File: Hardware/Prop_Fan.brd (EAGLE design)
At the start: 152.9 x 71.1 mm, 161 parts, among them J1 1546215-2, J2 1546215-2, J3 1546215-2, J4 1546215-2, J5 1546215-2, SW1 MF-SW-TACT-4.2MM, SW2 MF-SW-TACT-4.2MM, SW3 MF-SW-TACT-4.2MM, U1 P8X32A-Q44, U10 MAX31855KASA+, U11 MAX31855KASA+, U12 G3VM-61GR2(TR05), U13 G3VM-61GR2(TR05), U14 CD74HC595M96, U15 G3VM-61GR2(TR05), U16 CD74HC165M96, U17 G3VM-61GR2(TR05), U18 G3VM-61GR2(TR05), U19 G3VM-61GR2(TR05), U2 G3VM-61GR2(TR05), U20 G3VM-61GR2(TR05), U21 G3VM-61GR2(TR05), U22 G3VM-61GR2(TR05), U23 G3VM-61GR2(TR05), U24 G3VM-61GR2(TR05), U25 G3VM-61GR2(TR05), U26 G3VM-61GR2(TR05), U27 FXOS8700CQR1, U28 ACPL-C870-000E, U29 MAX11613EUA+, U3 G3VM-61GR2(TR05), U30 TPS7B6950QDBVRQ1, U4 MAX31855KASA+, U5 LM22678TJ-5.0/NOPB, U6 ADP3338AKCZ-3.3-RL, U7 CAT24C512WI-GT3, U8 G3VM-61GR2(TR05), U9 MAX31855KASA+, X1 ABMM-6.000MHZ-B2-T

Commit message: Fixed a couple traces and added camfiles.
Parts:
- added U$35: JEEP_LOGO_SILK_MEDIUM, PP_Aesthetics:JEEP_SILK_MEDIUM
- added U$42: LHE_LOGOLHE_LOGO, PP_Aesthetics:LHE_LOGO
- moved U$1 25.2 mm to (46.5, 15.2)
- moved TP2 12.4 mm to (20.3, 51.6)
- moved C22 3.05 mm to (23.4, 45.2)
- moved C23 3.05 mm to (23.4, 41.4)
- moved 3.3V_PWR 2.55 mm to (29.2, 39.4)
- moved R11 2.55 mm to (25.4, 39.4)
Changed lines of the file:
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@@
 <?xml version="1.0" encoding="utf-8"?>
 <!DOCTYPE eagle SYSTEM "eagle.dtd">
-<eagle version="7.4.0">
+<eagle version="6.6.0">
 <drawing>
 <settings>
@@
 <pass name="Default">
 <param name="RoutingGrid" value="50mil"/>
-<param name="AutoGrid" value="1"/>
-<param name="Efforts" value="0"/>
-<param name="TopRouterVariant" value="1"/>
 <param name="tpViaShape" value="round"/>
 <param name="PrefDir.1" value="|"/>
@@
 <attribute name="NAME" x="5.168" y="38.298" size="0.8128" layer="25" font="vector" ratio="16"/>
 </element>
-<element name="C22" library="PP_Passives" package="1210" value="10uF" x="23.436" y="48.21"/>
-<element name="C23" library="PP_Passives" package="0805" value="0.1uF" x="23.436" y="44.44"/>
+<element name="C22" library="PP_Passives" package="1210" value="10uF" x="23.436" y="45.162"/>
+<element name="C23" library="PP_Passives" package="0805" value="0.1uF" x="23.436" y="41.392"/>
 <element name="C24" library="PP_Passives" package="6.3MM_CAP_SMD" value="UWJ1C470MCL1GB" x="13.902" y="53.362" smashed="yes" rot="R270">
 <attribute name="NAME" x="10.648" y="56.895" size="0.8128" layer="25" font="vector" ratio="16"/>
 </element>
-<element name="3.3V_PWR" library="PP_LED" package="LED_0805" value="MF-LED-0805-RED" x="28.956" y="41.91" smashed="yes" rot="R180">
-<attribute name="NAME" x="26.585" y="43.18" size="0.8128" layer="25" font="vector" ratio="16"/>
-</element>
-<element name="R11" library="PP_Passives" package="0603" value="330" x="25.146" y="41.91" smashed="yes" rot="R180">
-<attribute name="NAME" x="23.5458" y="40.132" size="0.8128" layer="25" font="vector" ratio="16"/>
+<element name="3.3V_PWR" library="PP_LED" package="LED_0805" value="MF-LED-0805-RED" x="29.21" y="39.37" smashed="yes" rot="R180">
+<attribute name="NAME" x="26.839" y="40.64" size="0.8128" layer="25" font="vector" ratio="16"/>
+</element>
+<element name="R11" library="PP_Passives" package="0603" value="330" x="25.4" y="39.37" smashed="yes" rot="R180">
+<attribute name="NAME" x="21.2598" y="38.862" size="0.8128" layer="25" font="vector" ratio="16"/>
 </element>
 <element name="TP1" library="PP_Connectors" package="KEYSTONE_5115-5119" value="5115-5119" x="34.036" y="3.048" smashed="yes" rot="R90">
 <attribute name="NAME" x="33.02" y="5.842" size="0.8128" layer="25" font="vector" ratio="16"/>
 </element>
-<element name="TP2" library="PP_Connectors" package="KEYSTONE_5115-5119" value="5115-5119" x="20.574" y="39.116" smashed="yes">
-<attribute name="NAME" x="18.034" y="41.91" size="0.8128" layer="25" font="vector" ratio="16"/>
+<element name="TP2" library="PP_Connectors" package="KEYSTONE_5115-5119" value="5115-5119" x="20.32" y="51.562" smashed="yes">
+<attribute name="NAME" x="22.86" y="53.34" size="0.8128" layer="25" font="vector" ratio="16"/>
 </element>
 <element name="TP3" library="PP_Connectors" package="KEYSTONE_5115-5119" value="5115-5119" x="81.788" y="2.858" rot="R180"/>
@@
 </element>
 <element name="R15" library="PP_Passives" package="0805" value="10K" x="51.816" y="36.322" smashed="yes" rot="R270">
-<attribute name="NAME" x="48.768" y="36.83" size="0.8128" layer="25" font="vector" ratio="16"/>
+<attribute name="NAME" x="52.07" y="32.258" size="0.8128" layer="25" font="vector" ratio="16" rot="R90"/>
 </element>
 <element name="R16" library="PP_Passives" package="0805" value="10K" x="53.848" y="36.322" smashed="yes" rot="R270">
@@
 <element name="R10" library="PP_Passives" package="0805" value="10K" x="76.962" y="57.404" rot="R180"/>
 <element name="R17" library="PP_Passives" package="0805" value="10K" x="68.834" y="57.404" rot="R180"/>
-<element name="U$1" library="PP_Aesthetics" package="LHE_FRAME" value="LHE_FRAME" x="27.432" y="31.75">
-<attribute name="DNAME" value="Parker Dillmann" x="27.432" y="31.75" size="1.778" layer="27" display="off"/>
-<attribute name="REVNUM" value="REV: 1" x="27.432" y="31.75" size="1.778" layer="27" display="off"/>
+<element name="U$1" library="PP_Aesthetics" package="LHE_FRAME" value="LHE_FRAME" x="46.482" y="15.24">
+<attribute name="DNAME" value="Parker Dillmann" x="46.482" y="15.24" size="1.778" layer="27" display="off"/>
+<attribute name="REVNUM" value="REV: 1" x="46.482" y="15.24" size="1.778" layer="27" display="off"/>
 </element>
 <element name="FID1" library="MF_Aesthetics" package="FIDUCIAL_0.5MM" value="FIDUCIAL_0.5MM" x="7.62" y="60.198"/>
@@
 <element name="C45" library="PP_Passives" package="1210" value="10uF" x="149.352" y="32.004"/>
 <element name="U30" library="MF_IC_Power" package="SOT-23-5" value="TPS7B6950QDBVRQ1" x="149.352" y="27.94" rot="R90"/>
+<element name="U$35" library="PP_Aesthetics" package="JEEP_SILK_MEDIUM" value="JEEP_LOGO_SILK_MEDIUM" x="23.622" y="28.448"/>
+<element name="U$42" library="PP_Aesthetics" package="LHE_LOGO" value="LHE_LOGOLHE_LOGO" x="63.754" y="15.24"/>
 </elements>
 <signals>
@@
 <via x="11.938" y="40.386" extent="1-16" drill="0.5"/>
 <wire x1="11.938" y1="40.386" x2="11.938" y2="40.64" width="0.6096" layer="16"/>
-<wire x1="24.836" y1="48.21" x2="26.67" y2="48.21" width="0.6096" layer="1"/>
-<wire x1="26.67" y1="48.21" x2="26.67" y2="48.26" width="0.6096" layer="1"/>
-<via x="26.67" y="48.26" extent="1-16" drill="0.5"/>
-<wire x1="26.67" y1="48.26" x2="26.67" y2="48.514" width="0.6096" layer="16"/>
-<wire x1="24.336" y1="44.44" x2="25.654" y2="44.44" width="0.6096" layer="1"/>
-<wire x1="25.654" y1="44.44" x2="25.654" y2="44.45" width="0.6096" layer="1"/>
-<via x="25.654" y="44.45" extent="1-16" drill="0.5"/>
-<wire x1="25.654" y1="44.45" x2="25.654" y2="44.704" width="0.6096" layer="16"/>
+<wire x1="24.836" y1="45.162" x2="26.67" y2="45.162" width="0.6096" layer="1"/>
+<wire x1="26.67" y1="45.162" x2="26.67" y2="45.212" width="0.6096" layer="1"/>
+<via x="26.67" y="45.212" extent="1-16" drill="0.5"/>
+<wire x1="26.67" y1="45.212" x2="26.67" y2="45.466" width="0.6096" layer="16"/>
+<wire x1="24.336" y1="41.392" x2="25.654" y2="41.392" width="0.6096" layer="1"/>
+<wire x1="25.654" y1="41.392" x2="25.654" y2="41.402" width="0.6096" layer="1"/>
+<via x="25.654" y="41.402" extent="1-16" drill="0.5"/>
+<wire x1="25.654" y1="41.402" x2="25.654" y2="41.656" width="0.6096" layer="16"/>
 <polygon width="0.254" layer="1" isolate="0.3048" thermals="no">
 <vertex x="98.552" y="11.938"/>
@@
 <via x="77.724" y="14.351" extent="1-16" drill="0.5"/>
 <via x="77.724" y="15.621" extent="1-16" drill="0.5"/>
-<wire x1="30.006" y1="41.91" x2="31.242" y2="41.91" width="0.254" layer="1"/>
-<via x="31.242" y="41.91" extent="1-16" drill="0.5"/>
-<wire x1="31.242" y1="41.91" x2="31.242" y2="42.418" width="0.254" layer="16"/>
+<wire x1="30.26" y1="39.37" x2="31.496" y2="39.37" width="0.254" layer="1"/>
+<via x="31.496" y="39.37" extent="1-16" drill="0.5"/>
+<wire x1="31.496" y1="39.37" x2="31.496" y2="39.878" width="0.254" layer="16"/>
 <contactref element="C25" pad="2"/>
 <contactref element="U27" pad="P$16"/>
@@
 <vertex x="7.874" y="46.228"/>
 </polygon>
-<wire x1="24.296" y1="41.91" x2="22.606" y2="41.91" width="0.254" layer="1"/>
+<wire x1="24.55" y1="39.37" x2="22.606" y2="39.37" width="0.254" layer="1"/>
 <contactref element="U27" pad="P$1"/>
 <contactref element="C25" pad="1"/>
@@
 <wire x1="133.096" y1="34.29" x2="133.096" y2="34.925" width="0.254" layer="1"/>
 <polygon width="0.254" layer="16" thermals="no">
-<vertex x="20.512371875" y="38.1" curve="-90"/>
-<vertex x="19.558" y="39.054371875"/>
-<vertex x="19.558" y="50.437965625"/>
-<vertex x="26.778034375" y="57.658"/>
+<vertex x="24.13" y="56.642"/>
+<vertex x="25.508034375" y="57.912"/>
 <vertex x="90.424" y="57.658"/>
 <vertex x="93.472" y="54.61"/>
@@
 <vertex x="92.456" y="54.102"/>
 <vertex x="89.916" y="56.642"/>
-<vertex x="28.194" y="56.642"/>
-<vertex x="21.59" y="50.038"/>
-<vertex x="21.59" y="39.177628125" curve="-90"/>
 </polygon>
 <wire x1="41.148" y1="52.186" x2="37.222" y2="52.186" width="0.254" layer="1"/>
@@
 <wire x1="140.716" y1="39.37" x2="138.4935" y2="39.37" width="0.254" layer="16"/>
 <wire x1="138.4935" y1="39.37" x2="138.43" y2="39.4335" width="0.254" layer="16"/>
+<polygon width="0.254" layer="16" isolate="0.3048" thermals="no">
+<vertex x="25.4" y="57.912"/>
+<vertex x="19.53925625" y="52.05125625" curve="45"/>
+<vertex x="19.304" y="51.483296875" curve="90"/>
+<vertex x="20.241296875" y="50.546" curve="45"/>
+<vertex x="20.80925625" y="50.78125625"/>
+<vertex x="26.67" y="56.642"/>
+<vertex x="26.67" y="57.912"/>
+</polygon>
 </signal>
 <signal name="X1">
@@
 <contactref element="R11" pad="1"/>
 <contactref element="3.3V_PWR" pad="ANODE"/>
-<wire x1="25.996" y1="41.91" x2="27.906" y2="41.91" width="0.254" layer="1"/>
+<wire x1="26.25" y1="39.37" x2="28.16" y2="39.37" width="0.254" layer="1"/>
 </signal>
 <signal name="N$2">

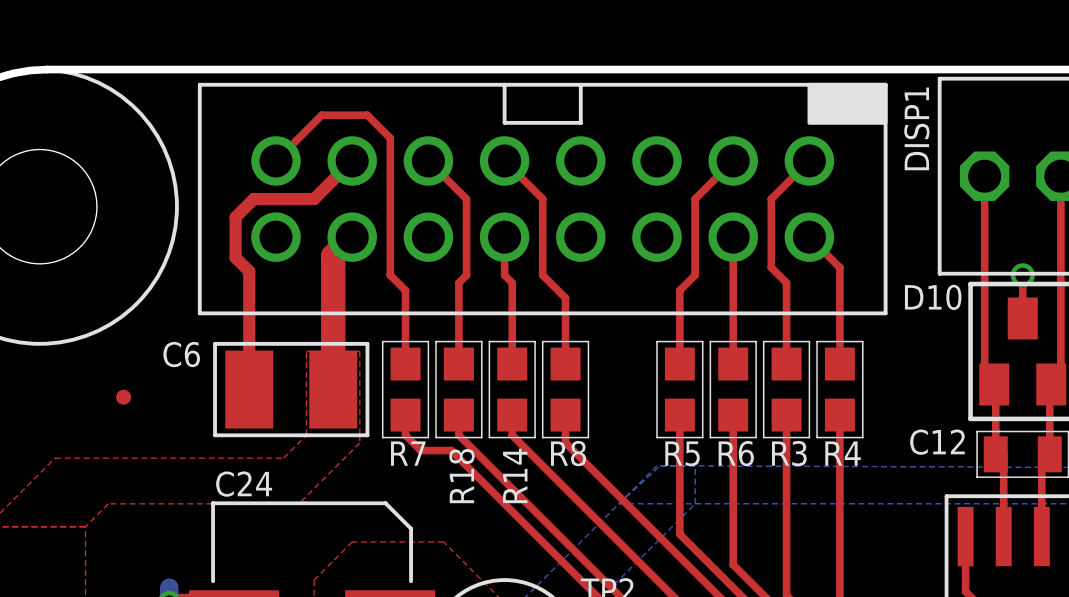
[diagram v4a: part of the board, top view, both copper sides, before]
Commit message: Fixed VFD connector. Was mirrored.
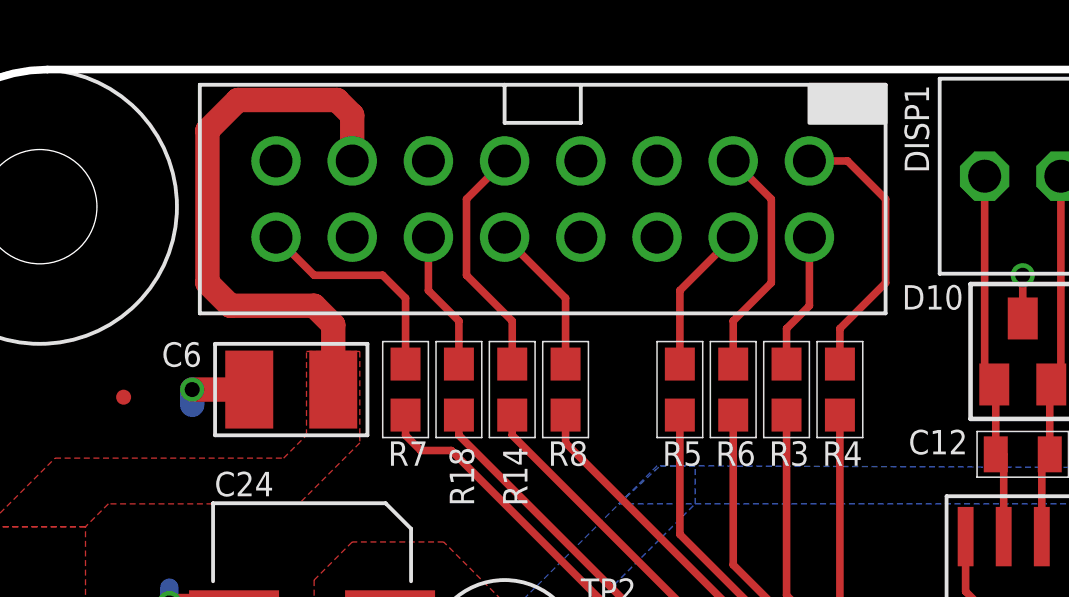
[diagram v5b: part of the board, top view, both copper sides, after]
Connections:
- net 5V_PWR: now also DISP1.P$13; no longer DISP1.P$14
- net D4: now also DISP1.P$3; no longer DISP1.P$4
- net D5: now also DISP1.P$4; no longer DISP1.P$3
- net D6: now also DISP1.P$1; no longer DISP1.P$2
- net D7: now also DISP1.P$2; no longer DISP1.P$1
- net E1: now also DISP1.P$10; no longer DISP1.P$9
- net E2: now also DISP1.P$16; no longer DISP1.P$15
- net GND: now also DISP1.P$14; no longer DISP1.P$13
- net R/W: now also DISP1.P$9; no longer DISP1.P$10
- net RS: now also DISP1.P$12; no longer DISP1.P$11
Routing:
- net 5V_PWR: track 14.7 -> 28.4 mm
- net GND: track 197.2 -> 189.0 mm, vias 138 -> 139
- net E2: track 12.5 -> 7.36 mm
- net D6: track 4.65 -> 9.20 mm
- net D4: track 4.23 -> 7.82 mm
- net R/W: track 4.34 -> 7.93 mm
- net D7: track 7.51 -> 4.55 mm
- net RS: track 7.40 -> 4.65 mm
- net D5: track 7.51 -> 4.97 mm
- net E1: track 7.61 -> 5.07 mm
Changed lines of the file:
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@@
 <?xml version="1.0" encoding="utf-8"?>
 <!DOCTYPE eagle SYSTEM "eagle.dtd">
-<eagle version="6.6.0">
+<eagle version="7.4.0">
 <drawing>
 <settings>
@@
 <pass name="Default">
 <param name="RoutingGrid" value="50mil"/>
+<param name="AutoGrid" value="1"/>
+<param name="Efforts" value="0"/>
+<param name="TopRouterVariant" value="1"/>
 <param name="tpViaShape" value="round"/>
 <param name="PrefDir.1" value="|"/>
@@
 <contactref element="PROP_UART" pad="1"/>
 <contactref element="PROP_TC" pad="P$5"/>
+<contactref element="DISP1" pad="P$7"/>
+<contactref element="DISP1" pad="P$5"/>
 <contactref element="DISP1" pad="P$8"/>
+<contactref element="DISP1" pad="P$14"/>
 <contactref element="DISP1" pad="P$6"/>
-<contactref element="DISP1" pad="P$7"/>
-<contactref element="DISP1" pad="P$13"/>
-<contactref element="DISP1" pad="P$5"/>
 <contactref element="C6" pad="2"/>
 <contactref element="U9" pad="1"/>
@@
 <via x="32.385" y="11.557" extent="1-16" drill="0.5"/>
 <via x="32.385" y="10.541" extent="1-16" drill="0.5"/>
-<wire x1="11.808" y1="60.452" x2="11.808" y2="64.392" width="0.4064" layer="1"/>
-<wire x1="11.808" y1="64.392" x2="11.35419375" y2="64.84580625" width="0.4064" layer="1"/>
-<wire x1="11.35419375" y1="64.84580625" x2="11.35419375" y2="66.19633125" width="0.4064" layer="1"/>
-<wire x1="11.35419375" y1="66.19633125" x2="11.9598625" y2="66.802" width="0.4064" layer="1"/>
-<wire x1="11.9598625" y1="66.802" x2="13.97" y2="66.802" width="0.4064" layer="1"/>
-<wire x1="13.97" y1="66.802" x2="15.24" y2="68.072" width="0.4064" layer="1"/>
 <wire x1="11.302" y1="53.362" x2="11.28" y2="53.34" width="0.6096" layer="1"/>
 <wire x1="11.28" y1="53.34" x2="9.144" y2="53.34" width="0.6096" layer="1"/>
@@
 <wire x1="143.637" y1="36.2835" x2="143.637" y2="34.417" width="0.254" layer="1"/>
 <wire x1="143.637" y1="34.417" x2="144.018" y2="34.036" width="0.254" layer="1"/>
+<wire x1="11.808" y1="60.452" x2="9.906" y2="60.452" width="0.8128" layer="1"/>
+<via x="9.906" y="60.452" extent="1-16" drill="0.5"/>
+<wire x1="9.906" y1="60.452" x2="9.906" y2="59.944" width="0.8128" layer="16"/>
 </signal>
 <signal name="3.3V">
@@
 <contactref element="L3" pad="1"/>
 <contactref element="U5" pad="P$6"/>
-<contactref element="DISP1" pad="P$14"/>
+<contactref element="DISP1" pad="P$13"/>
 <contactref element="C6" pad="1"/>
 <contactref element="C13" pad="1"/>
@@
 <wire x1="8.594" y1="37.79" x2="4.882" y2="37.79" width="0.8128" layer="1"/>
 <wire x1="4.882" y1="37.79" x2="4.826" y2="37.846" width="0.8128" layer="1"/>
-<wire x1="15.24" y1="65.532" x2="14.608" y2="64.9" width="0.8128" layer="1"/>
-<wire x1="14.608" y1="64.9" x2="14.608" y2="60.452" width="0.8128" layer="1"/>
 <polygon width="0.254" layer="1" isolate="0.3048" thermals="no">
 <vertex x="3.048" y="55.88"/>
@@
 <vertex x="6.35" y="55.88"/>
 </polygon>
+<wire x1="14.608" y1="60.452" x2="14.608" y2="62.608" width="0.8128" layer="1"/>
+<wire x1="14.608" y1="62.608" x2="13.97" y2="63.246" width="0.8128" layer="1"/>
+<wire x1="13.97" y1="63.246" x2="11.176" y2="63.246" width="0.8128" layer="1"/>
+<wire x1="11.176" y1="63.246" x2="10.414" y2="64.008" width="0.8128" layer="1"/>
+<wire x1="10.414" y1="64.008" x2="10.414" y2="69.088" width="0.8128" layer="1"/>
+<wire x1="10.414" y1="69.088" x2="11.43" y2="70.104" width="0.8128" layer="1"/>
+<wire x1="11.43" y1="70.104" x2="14.732" y2="70.104" width="0.8128" layer="1"/>
+<wire x1="14.732" y1="70.104" x2="15.24" y2="69.596" width="0.8128" layer="1"/>
+<wire x1="15.24" y1="69.596" x2="15.24" y2="68.072" width="0.8128" layer="1"/>
 </signal>
 <signal name="CHASSIS_GND">
@@
 </signal>
 <signal name="D7">
+<contactref element="DISP1" pad="P$2"/>
+<contactref element="R3" pad="2"/>
+<wire x1="29.718" y1="61.302" x2="29.718" y2="62.484" width="0.254" layer="1"/>
+<wire x1="29.718" y1="62.484" x2="30.48" y2="63.246" width="0.254" layer="1"/>
+<wire x1="30.48" y1="63.246" x2="30.48" y2="65.532" width="0.254" layer="1"/>
+</signal>
+<signal name="D6">
 <contactref element="DISP1" pad="P$1"/>
-<contactref element="R3" pad="2"/>
-<wire x1="29.718" y1="61.302" x2="29.718" y2="64.008" width="0.254" layer="1"/>
-<wire x1="29.718" y1="64.008" x2="29.21" y2="64.516" width="0.254" layer="1"/>
-<wire x1="29.21" y1="64.516" x2="29.21" y2="66.802" width="0.254" layer="1"/>
-<wire x1="29.21" y1="66.802" x2="30.48" y2="68.072" width="0.254" layer="1"/>
-</signal>
-<signal name="D6">
-<contactref element="DISP1" pad="P$2"/>
 <contactref element="R4" pad="2"/>
-<wire x1="31.496" y1="61.302" x2="31.496" y2="64.516" width="0.254" layer="1"/>
-<wire x1="31.496" y1="64.516" x2="30.48" y2="65.532" width="0.254" layer="1"/>
+<wire x1="31.496" y1="61.302" x2="31.496" y2="62.484" width="0.254" layer="1"/>
+<wire x1="31.496" y1="62.484" x2="33.02" y2="64.008" width="0.254" layer="1"/>
+<wire x1="33.02" y1="64.008" x2="33.02" y2="66.802" width="0.254" layer="1"/>
+<wire x1="33.02" y1="66.802" x2="31.75" y2="68.072" width="0.254" layer="1"/>
+<wire x1="31.75" y1="68.072" x2="30.48" y2="68.072" width="0.254" layer="1"/>
 </signal>
 <signal name="D5">
-<contactref element="DISP1" pad="P$3"/>
+<contactref element="DISP1" pad="P$4"/>
 <contactref element="R5" pad="2"/>
 <wire x1="26.162" y1="61.302" x2="26.162" y2="63.754" width="0.254" layer="1"/>
-<wire x1="26.162" y1="63.754" x2="26.67" y2="64.262" width="0.254" layer="1"/>
-<wire x1="26.67" y1="64.262" x2="26.67" y2="66.802" width="0.254" layer="1"/>
-<wire x1="26.67" y1="66.802" x2="27.94" y2="68.072" width="0.254" layer="1"/>
+<wire x1="26.162" y1="63.754" x2="27.94" y2="65.532" width="0.254" layer="1"/>
 </signal>
 <signal name="D4">
-<contactref element="DISP1" pad="P$4"/>
+<contactref element="DISP1" pad="P$3"/>
 <contactref element="R6" pad="2"/>
-<wire x1="27.94" y1="61.302" x2="27.94" y2="65.532" width="0.254" layer="1"/>
+<wire x1="27.94" y1="61.302" x2="27.94" y2="62.738" width="0.254" layer="1"/>
+<wire x1="27.94" y1="62.738" x2="29.21" y2="64.008" width="0.254" layer="1"/>
+<wire x1="29.21" y1="64.008" x2="29.21" y2="66.802" width="0.254" layer="1"/>
+<wire x1="29.21" y1="66.802" x2="27.94" y2="68.072" width="0.254" layer="1"/>
 </signal>
 <signal name="E2">
-<contactref element="DISP1" pad="P$15"/>
+<contactref element="DISP1" pad="P$16"/>
 <contactref element="R7" pad="2"/>
-<wire x1="12.7" y1="68.072" x2="14.224" y2="69.596" width="0.254" layer="1"/>
-<wire x1="14.224" y1="69.596" x2="15.748" y2="69.596" width="0.254" layer="1"/>
-<wire x1="15.748" y1="69.596" x2="16.51" y2="68.834" width="0.254" layer="1"/>
-<wire x1="16.51" y1="68.834" x2="16.51" y2="64.262" width="0.254" layer="1"/>
-<wire x1="16.51" y1="64.262" x2="17.018" y2="63.754" width="0.254" layer="1"/>
-<wire x1="17.018" y1="63.754" x2="17.018" y2="61.302" width="0.254" layer="1"/>
+<wire x1="17.018" y1="61.302" x2="17.018" y2="63.5" width="0.254" layer="1"/>
+<wire x1="17.018" y1="63.5" x2="16.256" y2="64.262" width="0.254" layer="1"/>
+<wire x1="16.256" y1="64.262" x2="13.97" y2="64.262" width="0.254" layer="1"/>
+<wire x1="13.97" y1="64.262" x2="12.7" y2="65.532" width="0.254" layer="1"/>
 </signal>
 <signal name="E1">
-<contactref element="DISP1" pad="P$9"/>
+<contactref element="DISP1" pad="P$10"/>
 <contactref element="R8" pad="2"/>
 <wire x1="22.352" y1="61.302" x2="22.352" y2="63.5" width="0.254" layer="1"/>
-<wire x1="22.352" y1="63.5" x2="21.59" y2="64.262" width="0.254" layer="1"/>
-<wire x1="21.59" y1="64.262" x2="21.59" y2="66.802" width="0.254" layer="1"/>
-<wire x1="21.59" y1="66.802" x2="20.32" y2="68.072" width="0.254" layer="1"/>
+<wire x1="22.352" y1="63.5" x2="20.32" y2="65.532" width="0.254" layer="1"/>
 </signal>
 <signal name="R/W">
-<contactref element="DISP1" pad="P$10"/>
+<contactref element="DISP1" pad="P$9"/>
 <contactref element="R14" pad="2"/>
-<wire x1="20.574" y1="61.302" x2="20.574" y2="64.008" width="0.254" layer="1"/>
-<wire x1="20.574" y1="64.008" x2="20.32" y2="64.262" width="0.254" layer="1"/>
-<wire x1="20.32" y1="64.262" x2="20.32" y2="65.532" width="0.254" layer="1"/>
+<wire x1="20.574" y1="61.302" x2="20.574" y2="62.738" width="0.254" layer="1"/>
+<wire x1="20.574" y1="62.738" x2="19.05" y2="64.262" width="0.254" layer="1"/>
+<wire x1="19.05" y1="64.262" x2="19.05" y2="66.802" width="0.254" layer="1"/>
+<wire x1="19.05" y1="66.802" x2="20.32" y2="68.072" width="0.254" layer="1"/>
 </signal>
 <signal name="RS">
-<contactref element="DISP1" pad="P$11"/>
+<contactref element="DISP1" pad="P$12"/>
 <contactref element="R18" pad="2"/>
-<wire x1="18.796" y1="61.302" x2="18.796" y2="64.008" width="0.254" layer="1"/>
-<wire x1="18.796" y1="64.008" x2="19.05" y2="64.262" width="0.254" layer="1"/>
-<wire x1="19.05" y1="64.262" x2="19.05" y2="66.802" width="0.254" layer="1"/>
-<wire x1="19.05" y1="66.802" x2="17.78" y2="68.072" width="0.254" layer="1"/>
+<wire x1="18.796" y1="61.302" x2="18.796" y2="62.738" width="0.254" layer="1"/>
+<wire x1="18.796" y1="62.738" x2="17.78" y2="63.754" width="0.254" layer="1"/>
+<wire x1="17.78" y1="63.754" x2="17.78" y2="65.532" width="0.254" layer="1"/>
 </signal>
 <signal name="PROP_D7">
